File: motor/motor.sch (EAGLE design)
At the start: 91 parts, among them IC1 FT231XQ, P1 MF-NSML600-2, Q3 BSS138, Q4 BSS138, T1 TRANSISTORMMBT2222, T2 TRANSISTORMMBT2222, T3 TRANSISTORMMBT2222

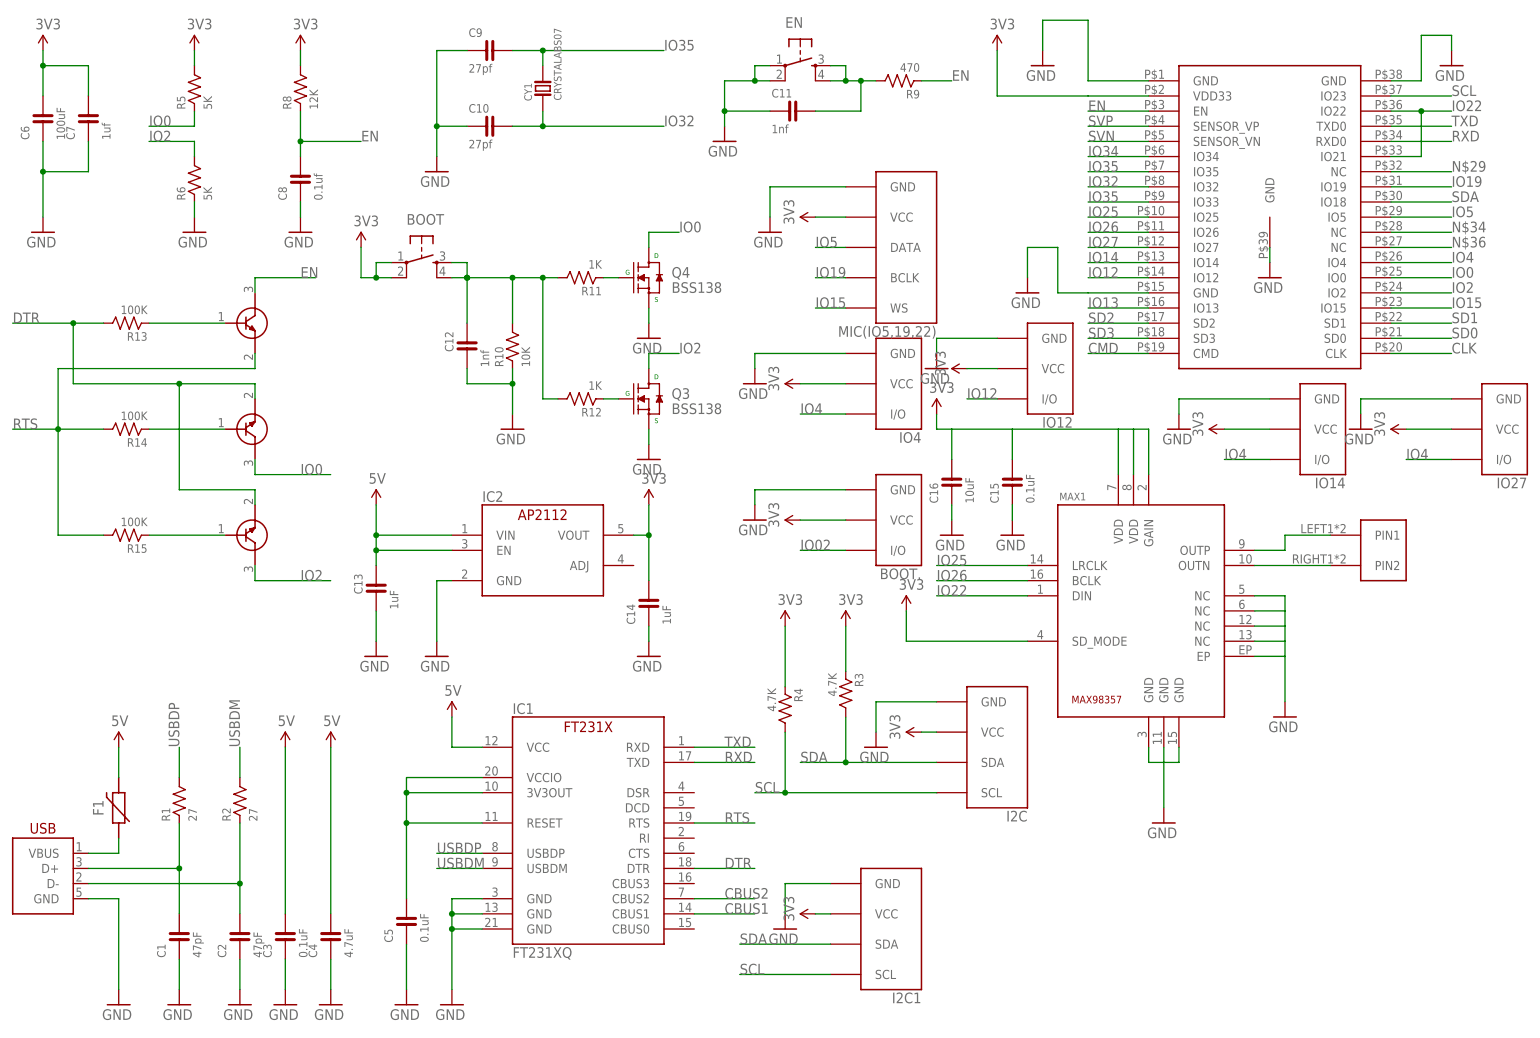
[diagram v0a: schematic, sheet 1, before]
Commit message: Update motor.
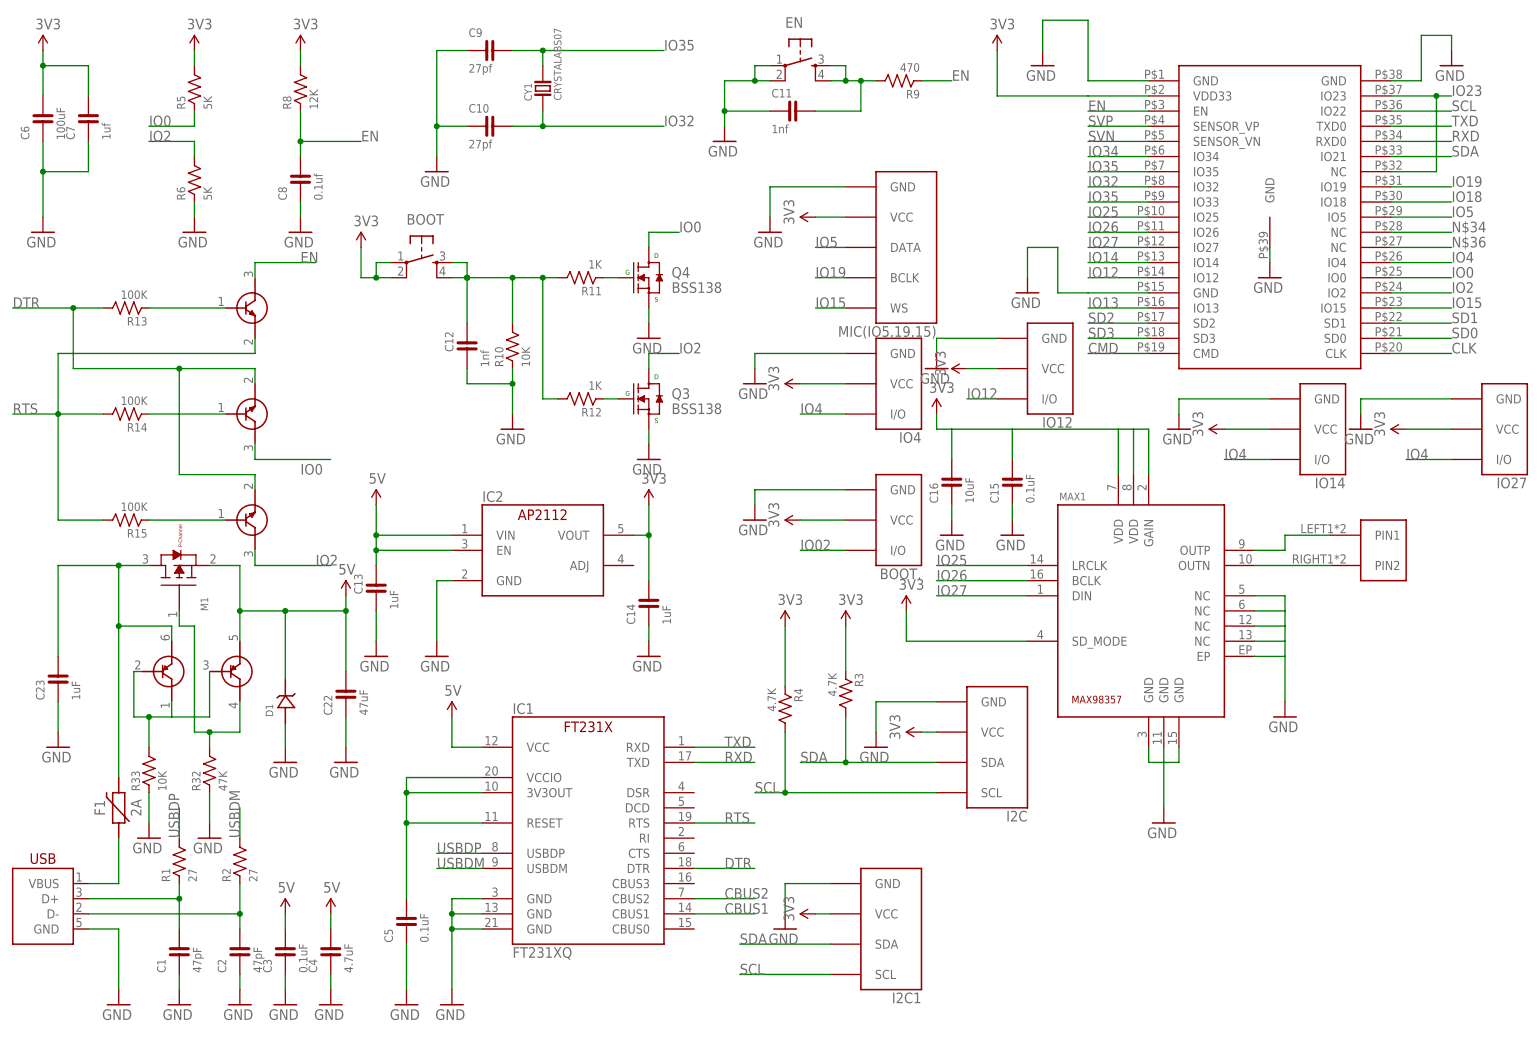
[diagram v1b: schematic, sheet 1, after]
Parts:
- added C22: 47uF, FaBo-Capacitor:CAPACITOR-0603_NARROW
- added C23: 1uF, FaBo-Capacitor:CAPACITOR-0603_NARROW
- added D1: (no value), FaBo-Diode:SMBJ5.0
- added M1: (no value), FaBo-Mosfet:MOSFET-P_DMG2305UX
- added R32: 47K, FaBo-Resistors:RESISTOR-0603-NARROW
- added R33: 10K, FaBo-Resistors:RESISTOR-0603-NARROW
- added U$6: DUAL-PNP-TRANSISTORDMMT5401, FaBo-Transistor:DUAL-PNP-TRANSISTORDMMT5401
- F1: value (none) -> 2A
- R24, R25: device FaBo-Resistors:RESISTOR-0402 -> FaBo-Resistors:RESISTOR-0603
- renumbered MIC(IO5,19,22) to MIC(IO5,19,15)
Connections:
- removed net IO22: MAX1.DIN, U$1.IO21, U$1.IO22
- removed net N$29: U$1.NC@32
- new net IO18: U$1.IO18
- new net IO23: U$1.IO23, U$1.NC@32
- new net N$16: C23.2, F1.2, M1.D, U$6.E1
- new net N$17: M1.G, R32.2, U$6.C2
- new net N$26: R33.2, U$6.B1, U$6.B2, U$6.C1
- net 5V: now also C22.2, D1.ANODE, M1.S, U$6.E2; no longer F1.2
- net GND: now also C22.1, C23.1, D1.CATHODE, R32.1, R33.1
- net IO27: now also MAX1.DIN
- net SCL: now also U$1.IO22; no longer U$1.IO23
- net SDA: now also U$1.IO21; no longer U$1.IO18
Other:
- moved on the sheet: C1, C2, C3, C4, R1, R13, R14, R15, R2

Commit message: Update motor.
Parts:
- removed S1: STPS15L30CB, FaBo-Supply:STPS15L30C
- added C24: 47uF, FaBo-Capacitor:CAPACITOR-0603_NARROW
- added C25: 1uF, FaBo-Capacitor:CAPACITOR-0603_NARROW
- added D2: (no value), FaBo-Diode:SMBJ5.0
- added M2: (no value), FaBo-Mosfet:MOSFET-P_DMG2305UX
- added R34: 47K, FaBo-Resistors:RESISTOR-0603-NARROW
- added R35: 10K, FaBo-Resistors:RESISTOR-0603-NARROW
- added U$7: DUAL-PNP-TRANSISTORDMMT5401, FaBo-Transistor:DUAL-PNP-TRANSISTORDMMT5401
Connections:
- removed net VCC: A5.+, C17.2, C18.2, C20.2, PWM0.VCC, PWM1.VCC, PWM2.VCC, PWM3.VCC, PWM4.VCC, PWM5.VCC, S1.K, U$8.VCC
- new net N$29: M2.G, R34.2, U$7.C2
- new net N$30: R35.2, U$7.B1, U$7.B2, U$7.C1
- net 5V: now also A5.+, C17.2, C18.2, C20.2, C24.2, D2.ANODE, M2.S, PWM0.VCC, PWM1.VCC, PWM2.VCC, PWM3.VCC, PWM4.VCC, PWM5.VCC, U$7.E2, U$8.VCC
- net GND: now also C24.1, C25.1, D2.CATHODE, R34.1, R35.1
- net N$28: now also C25.2, M2.D, U$7.E1; no longer S1.A1, S1.A2
